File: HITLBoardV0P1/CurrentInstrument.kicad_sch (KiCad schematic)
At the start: 33 parts, among them U22 TLV4387PWR, U23 ADS131M04QPWRQ1

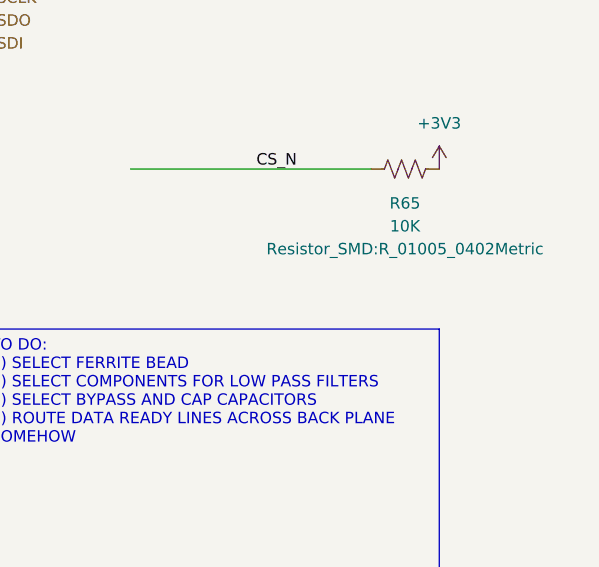
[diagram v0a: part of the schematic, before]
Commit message: ADD GPIO EXPANDER FOR RPI PICO
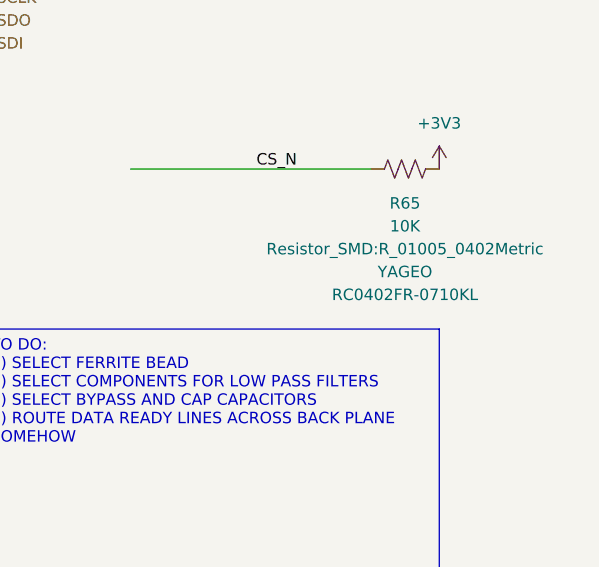
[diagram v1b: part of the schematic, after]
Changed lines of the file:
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@@
 		)
 		(property "MFG" "YAGEO"
-			(at 250.19 204.47 90)
-			(hide yes)
+			(at 250.19 215.9 90)
 			(show_name no)
 			(do_not_autoplace no)
@@
 		)
 		(property "MPN" "RC0402FR-0710KL"
-			(at 250.19 204.47 90)
-			(hide yes)
+			(at 250.19 218.44 90)
 			(show_name no)
 			(do_not_autoplace no)

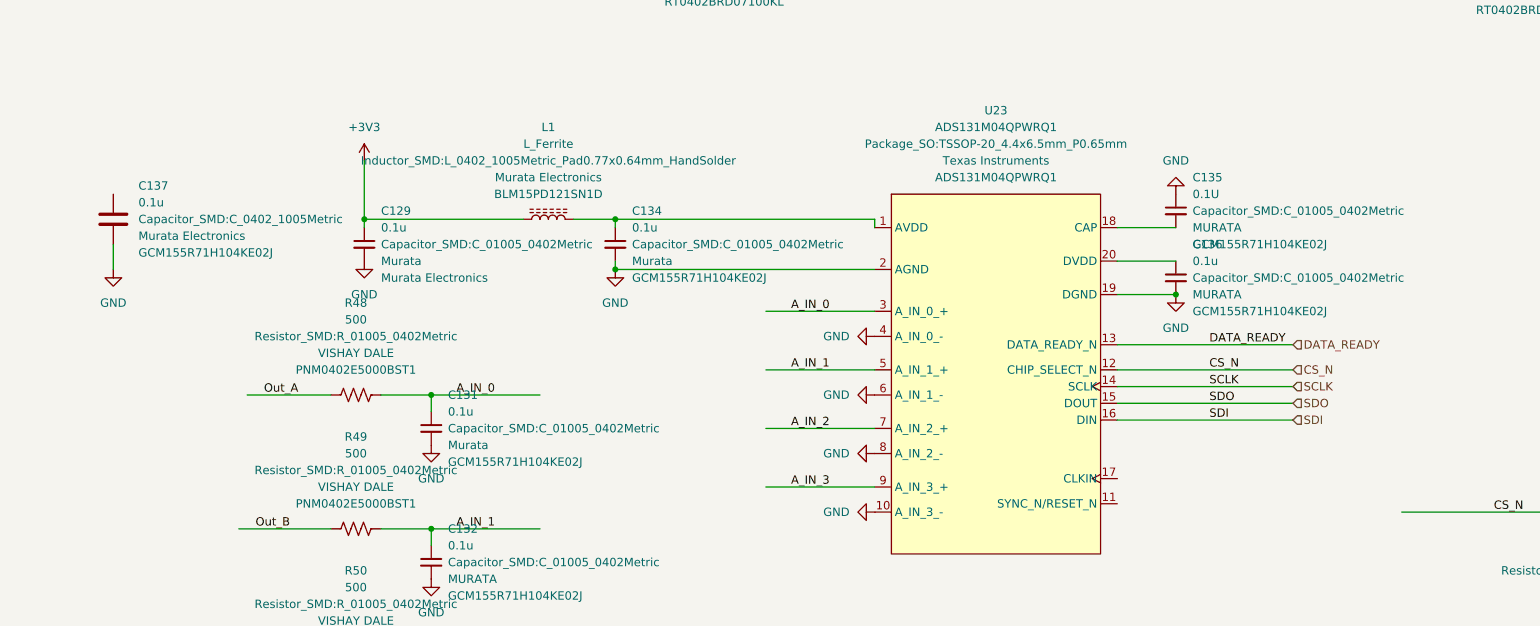
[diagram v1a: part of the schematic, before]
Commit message: FIX spi 3 on tmdx for current loop ADC, add gpio pin for data ready
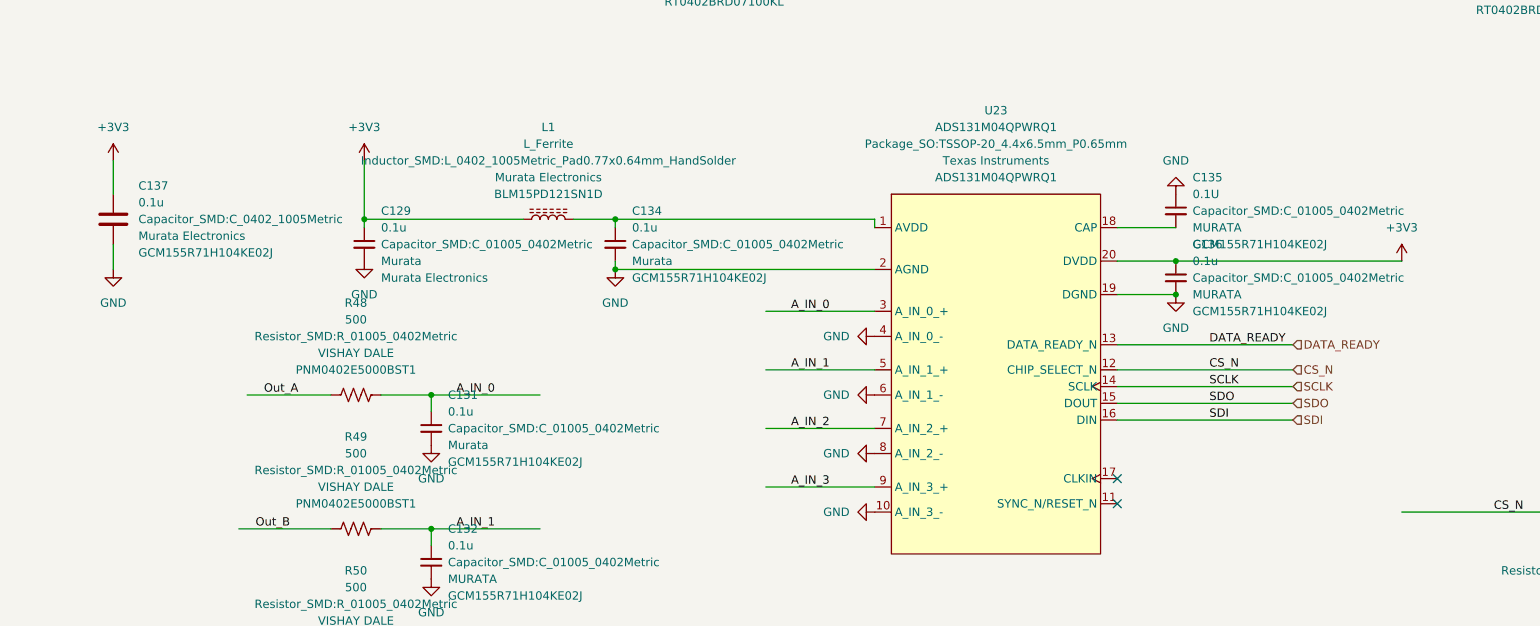
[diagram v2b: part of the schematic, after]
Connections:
- net +3V3: now also C136.1, C137.1, U23.20 (DVDD)
- no-connect marks 0 -> 2
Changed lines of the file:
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@@
 	)
 	(junction
+		(at 185.42 166.37)
+		(diameter 0)
+		(color 0 0 0 0)
+	)
+	(junction
 		(at 71.12 247.65)
 		(diameter 0)
@@
 		(color 0 0 0 0)
 	)
+	(no_connect
+		(at 176.53 199.39)
+	)
+	(no_connect
+		(at 176.53 203.2)
+	)
 	(wire
 		(pts
@@
 	(wire
 		(pts
+			(xy 24.13 151.13) (xy 24.13 156.21)
+		)
+		(stroke
+			(width 0)
+			(type default)
+		)
+	)
+	(wire
+		(pts
 			(xy 123.19 200.66) (xy 139.7 200.66)
 		)
@@
 	(wire
 		(pts
+			(xy 185.42 166.37) (xy 219.71 166.37)
+		)
+		(stroke
+			(width 0)
+			(type default)
+		)
+	)
+	(wire
+		(pts
 			(xy 72.39 227.33) (xy 72.39 229.87)
 		)
@@
 	)
 	(symbol
+		(lib_id "power:+3V3")
+		(at 219.71 166.37 0)
+		(unit 1)
+		(body_style 1)
+		(exclude_from_sim no)
+		(in_bom yes)
+		(on_board yes)
+		(in_pos_files yes)
+		(dnp no)
+		(fields_autoplaced yes)
+		(property "Reference" "#PWR0335"
+			(at 219.71 170.18 0)
+			(hide yes)
+			(show_name no)
+			(do_not_autoplace no)
+			(effects
+				(font
+					(size 1.27 1.27)
+				)
+			)
+		)
+		(property "Value" "+3V3"
+			(at 219.71 161.29 0)
+			(show_name no)
+			(do_not_autoplace no)
+			(effects
+				(font
+					(size 1.27 1.27)
+				)
+			)
+		)
+		(property "Footprint" ""
+			(at 219.71 166.37 0)
+			(hide yes)
+			(show_name no)
+			(do_not_autoplace no)
+			(effects
+				(font
+					(size 1.27 1.27)
+				)
+			)
+		)
+		(property "Datasheet" ""
+			(at 219.71 166.37 0)
+			(hide yes)
+			(show_name no)
+			(do_not_autoplace no)
+			(effects
+				(font
+					(size 1.27 1.27)
+				)
+			)
+		)
+		(property "Description" "Power symbol creates a global label with name \"+3V3\""
+			(at 219.71 166.37 0)
+			(hide yes)
+			(show_name no)
+			(do_not_autoplace no)
+			(effects
+				(font
+					(size 1.27 1.27)
+				)
+			)
+		)
+		(pin "1"
+		)
+		(instances
+			(project "HITLBoardV0P1"
+				(path "/ef043e91-6391-40b5-b326-2e3f2f5d4c07/6e0acfce-3923-4d65-b62d-541c4a9771e5"
+					(reference "#PWR0335")
+					(unit 1)
+				)
+			)
+		)
+	)
+	(symbol
 		(lib_id "power:GND")
 		(at 139.7 177.8 270)
@@
 					(unit 1)
 				)
+			)
+		)
+	)
+	(symbol
+		(lib_id "power:+3V3")
+		(at 24.13 151.13 0)
+		(unit 1)
+		(body_style 1)
+		(exclude_from_sim no)
+		(in_bom yes)
+		(on_board yes)
+		(in_pos_files yes)
+		(dnp no)
+		(fields_autoplaced yes)
+		(property "Reference" "#PWR0334"
+			(at 24.13 154.94 0)
+			(hide yes)
+			(show_name no)
+			(do_not_autoplace no)
+			(effects
+				(font
+					(size 1.27 1.27)
+				)
+			)
+		)
+		(property "Value" "+3V3"
+			(at 24.13 146.05 0)
+			(show_name no)
+			(do_not_autoplace no)
+			(effects
+				(font
+					(size 1.27 1.27)
+				)
+			)
+		)
+		(property "Footprint" ""
+			(at 24.13 151.13 0)
+			(hide yes)
+			(show_name no)
+			(do_not_autoplace no)
+			(effects
+				(font
+					(size 1.27 1.27)
+				)
+			)
+		)
+		(property "Datasheet" ""
+			(at 24.13 151.13 0)
+			(hide yes)
+			(show_name no)
+			(do_not_autoplace no)
+			(effects
+				(font
+					(size 1.27 1.27)
+				)
+			)
+		)
+		(property "Description" "Power symbol creates a global label with name \"+3V3\""
+			(at 24.13 151.13 0)
+			(hide yes)
+			(show_name no)
+			(do_not_autoplace no)
+			(effects
+				(font
+					(size 1.27 1.27)
+				)
+			)
+		)
+		(pin "1"
+		)
+		(instances
+			(project "HITLBoardV0P1"
+				(path "/ef043e91-6391-40b5-b326-2e3f2f5d4c07/6e0acfce-3923-4d65-b62d-541c4a9771e5"
+					(reference "#PWR0334")
+					(unit 1)
+				)
